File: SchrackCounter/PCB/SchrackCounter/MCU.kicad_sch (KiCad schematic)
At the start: 0 parts

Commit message: update
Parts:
- added C?: 100nF.mcu, Capacitor_SMD:C_0805_2012Metric_Pad1.18x1.45mm_HandSolder, symbol Device:C
- added C?: 10uF.mcu, Capacitor_Tantalum_SMD:CP_EIA-3216-18_Kemet-A_Pad1.58x1.35mm_HandSolder, symbol Device:C_Polarized
- added U?: ESP32-S3-WROOM-1, PCM_Espressif:ESP32-S3-WROOM-1, symbol sumec_sch_lib:ESP32-S3-WROOM-1_CUSTOM_made_by_bismarx
- added U?: ESP32-S3-WROOM-2, PCM_Espressif:ESP32-S3-WROOM-2, symbol PCM_Espressif:ESP32-S3-WROOM-2
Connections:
- new net: U?.1 (GND), U?.40 (GND), U?.41 (GND)
- new net +3V3: C?.1, C?.1, U?.2 (3V3)
- new net BOOT: U?.27 (IO0)
- new net D+: U?.14 (IO20)
- new net D-: U?.13 (IO19)
- new net EN: U?.3 (EN)
- new net GND: C?.2, C?.2, U?.1 (GND), U?.40 (GND), U?.41 (GND)
- new net IN1: U?.33 (IO40)
- new net IN2: U?.34 (IO41)
- new net IPROPI_ADC: U?.29 (IO36)
- new net IR MODULE: U?.28 (IO35)
- new net LED1: U?.23 (IO21)
- new net LED2: U?.22 (IO14)
- new net LED3: U?.21 (IO13)
- new net OUT 1A: U?.18 (IO10)
- new net OUT 1B: U?.17 (IO9)
- new net OUT 2A: U?.19 (IO11)
- new net OUT 2B: U?.20 (IO12)
- new net POL 1: U?.5 (IO5)
- new net POL 2: U?.8 (IO15)
- new net POL 3: U?.9 (IO16)
- new net PWM1: U?.35 (IO42)
- new net PWM2: U?.32 (IO39)
- new net QRE1113 A: U?.6 (IO6)
- new net QRE1113 B: U?.7 (IO7)
- new net QRE1113 C: U?.38 (IO2)
- new net RX: U?.36 (RXD0)
- new net SCL: U?.11 (IO18)
- new net SDA: U?.10 (IO17)
- new net SHARP 1: U?.12 (IO8)
- new net SHARP 2: U?.4 (IO4)
- new net TEST PROGRAM 1: U?.25 (IO48)
- new net TEST PROGRAM 2: U?.24 (IO47)
- new net TX: U?.37 (TXD0)
- new net nFAULT: U?.30 (IO37)
- new net nSLEEP: U?.31 (IO38)
- no-connect marks 0 -> 3
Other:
- note added: "Default Configuration of Strapping Pins Strapping Pin Default Configuration Bit Value GPIO0 Pull-up 1 GPIO3 Floating - GPIO45 Pull-down 0 GPIO46 Pull-down 0"
- note added: "ESP32-S3 Datasheet"
- note added: "ESP32-S3-WROOM1-N4"
- note added: "GPIO0 has an internal pullup resistor, so if it is left unconnected then it will pull high."
- note added: "GPIO0, GPIO45, and GPIO46 are connected to the chip's internal weak pull-up/pull-down resistors at chip reset. These resistors determine the default bit values of the strapping pins. Also, these resistors determine the bit values if the strapping pins are connected to an external high-impedance circuit."
- note added: "TEST!!!"
- note added: "Typically these can be used, but you need to make sure they are not in the wrong state during boot. gpio.0 Boot Mode. Weak pullup during reset. (Boot Mode 0=Boot from Flash, 1=Download) gpio.3 JTAG Mode. Weak pull down during reset. (JTAG Config) gpio.45 SPI voltage. Weak pull down during reset. (SPI Voltage 0=3.3v 1=1.8v) gpio.46 Boot mode. Weak pull down during reset. (Enabling/Disabling ROM Me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"
- note added: "working voltage for pins 47 and 48 is 1.8 (test it) Check pins with datasheet, ADC, SP, USB etc Check encoder connection UART connection?"

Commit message: Schematic update
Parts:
- removed U?: ESP32-S3-WROOM-1, PCM_Espressif:ESP32-S3-WROOM-1, symbol sumec_sch_lib:ESP32-S3-WROOM-1_CUSTOM_made_by_bismarx
- removed U?: ESP32-S3-WROOM-2, PCM_Espressif:ESP32-S3-WROOM-2, symbol PCM_Espressif:ESP32-S3-WROOM-2
- added U7: ESP32-S3-WROOM-2, PCM_Espressif:ESP32-S3-WROOM-2, symbol sumec_sch_lib:ESP32-S3-WROOM-2_CUSTOM_made_by_bismarx
- gave numbers to parts that had none: 2
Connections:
- net +3V3: now also U7.2 (3V3)
- net BOOT: now also U7.27 (IO0)
- net EN: now also U7.3 (EN)
- net GND: now also U7.1 (GND), U7.40 (GND), U7.41 (GND)
- no-connect marks 3 -> 2
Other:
- note removed: "TEST!!!"
- moved on the sheet: C11, C12

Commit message: Schematic update
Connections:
- net D-: now reaches U7.13 (IO19)
- net D+: now reaches U7.14 (IO20)
- net ~{CS}: now reaches U7.18 (IO10)
- net MOSI: now reaches U7.19 (IO11)
- net CLK: now reaches U7.20 (IO12)
- net RX: now reaches U7.36 (RXD0)
- net TX: now reaches U7.37 (TXD0)
- no-connect marks 2 -> 3
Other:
- note added: "ESP32-S3-WROOM2"
- note removed: "ESP32-S3-WROOM1-N4"
- note removed: "working voltage for pins 47 and 48 is 1.8 (test it) Check pins with datasheet, ADC, SP, USB etc Check encoder connection UART connection?"
- moved on the sheet: C11, C12, U7

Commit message: sleep, overated imo
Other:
- note added: "GPIO0 has an internal pullup resistor, so if it is left unconnected then it will pull high. GPIO0, GPIO45, and GPIO46 are connected to the chip's internal weak pull-up/pull-down resistors at chip reset. These resistors determine the default bit values of the strapping pins. Also, these resistors determine the bit values if the strapping pins are connected to an external high-impedance circuit."
- note removed: "GPIO0 has an internal pullup resistor, so if it is left unconnected then it will pull high."
- note removed: "GPIO0, GPIO45, and GPIO46 are connected to the chip's internal weak pull-up/pull-down resistors at chip reset. These resistors determine the default bit values of the strapping pins. Also, these resistors determine the bit values if the strapping pins are connected to an external high-impedance circuit."
- moved on the sheet: C11, C12, U7

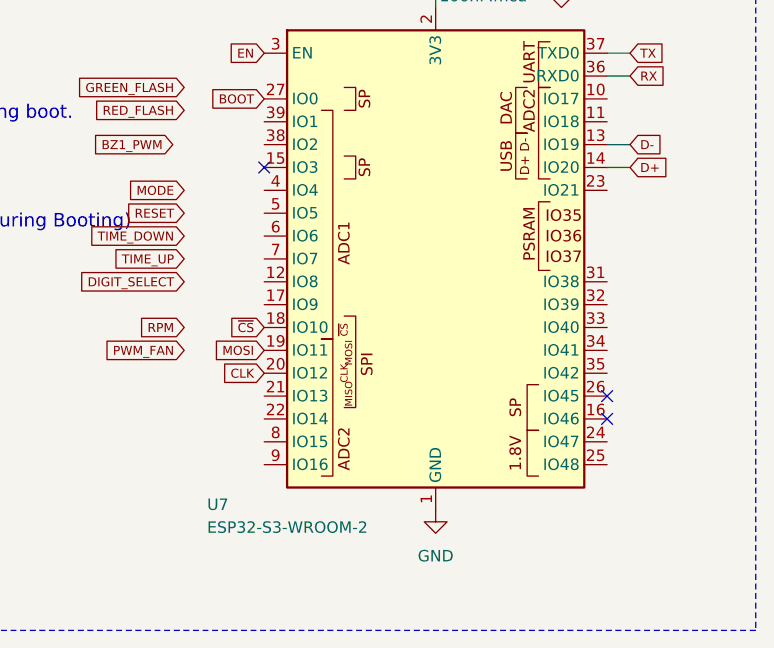
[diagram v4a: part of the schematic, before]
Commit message: SD card addition
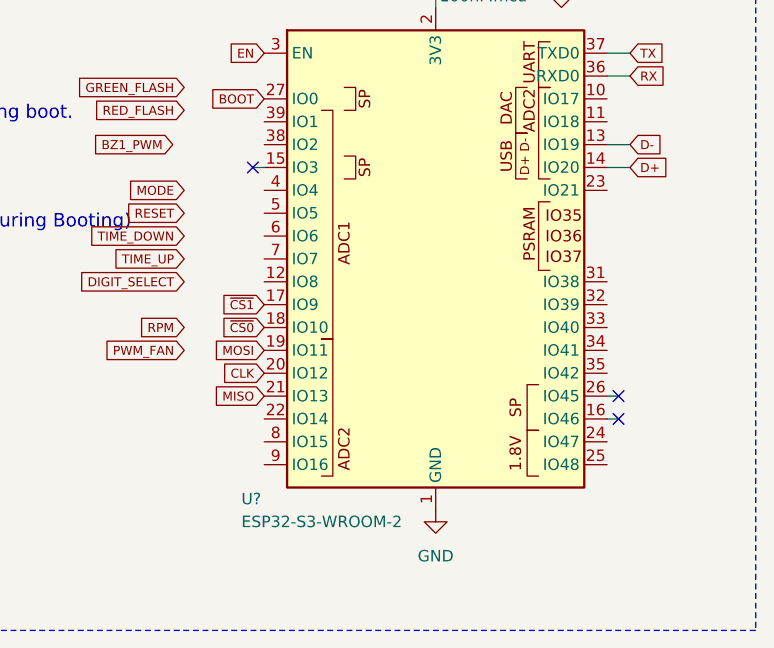
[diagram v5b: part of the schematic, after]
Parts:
- removed U7: ESP32-S3-WROOM-2, PCM_Espressif:ESP32-S3-WROOM-2, symbol sumec_sch_lib:ESP32-S3-WROOM-2_CUSTOM_made_by_bismarx
- added U?: ESP32-S3-WROOM-2, PCM_Espressif:ESP32-S3-WROOM-2, symbol sumec_sch_lib:ESP32-S3-WROOM-2_CUSTOM_made_by_bismarx
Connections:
- net +3V3: now also U?.2 (3V3)
- net BOOT: now also U?.27 (IO0)
- net CLK: now also U?.20 (IO12)
- net D+: now also U?.14 (IO20)
- net D-: now also U?.13 (IO19)
- net EN: now also U?.3 (EN)
- net GND: now also U?.1 (GND), U?.40 (GND), U?.41 (GND)
- net MOSI: now also U?.19 (IO11)
- net RX: now also U?.36 (RXD0)
- net TX: now also U?.37 (TXD0)
- new net MISO: U?.21 (IO13)
- new net ~{CS0}: U?.18 (IO10)
- new net ~{CS1}: U?.17 (IO9)
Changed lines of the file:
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@@
 	)
 	(no_connect
-		(at 217.17 114.3)
+		(at 218.44 114.3)
 	)
 	(no_connect
-		(at 179.07 86.36)
+		(at 177.8 86.36)
 	)
 	(no_connect
-		(at 217.17 111.76)
+		(at 218.44 111.76)
 	)
 	(wire
@@
 	(wire
 		(pts
+			(xy 218.44 111.76) (xy 217.17 111.76)
+		)
+		(stroke
+			(width 0)
+			(type default)
+		)
+	)
+	(wire
+		(pts
 			(xy 198.12 55.88) (xy 198.12 63.5)
 		)
@@
 		(pts
 			(xy 198.12 53.34) (xy 198.12 55.88)
+		)
+		(stroke
+			(width 0)
+			(type default)
+		)
+	)
+	(wire
+		(pts
+			(xy 177.8 86.36) (xy 179.07 86.36)
+		)
+		(stroke
+			(width 0)
+			(type default)
+		)
+	)
+	(wire
+		(pts
+			(xy 218.44 114.3) (xy 217.17 114.3)
 		)
 		(stroke
@@
 		)
 	)
-	(global_label "~{CS}"
+	(global_label "~{CS0}"
 		(shape input)
 		(at 179.07 104.14 180)
@@
 		)
 		(property "Intersheetrefs" "${INTERSHEET_REFS}"
-			(at 175.1948 104.14 0)
+			(at 174.4504 104.14 0)
 			(effects
 				(font
@@
 		)
 	)
+	(global_label "~{CS1}"
+		(shape input)
+		(at 179.07 101.6 180)
+		(fields_autoplaced yes)
+		(effects
+			(font
+				(face "Bahnschrift")
+				(size 1 1)
+				(color 0 0 0 1)
+			)
+			(justify right)
+		)
+		(property "Intersheetrefs" "${INTERSHEET_REFS}"
+			(at 174.7298 101.6 0)
+			(effects
+				(font
+					(size 1.27 1.27)
+				)
+				(justify right)
+				(hide yes)
+			)
+		)
+	)
 	(global_label "DIGIT_SELECT"
 		(shape input)
@@
 		)
 	)
+	(global_label "MISO"
+		(shape input)
+		(at 179.07 111.76 180)
+		(fields_autoplaced yes)
+		(effects
+			(font
+				(face "Bahnschrift")
+				(size 1 1)
+				(color 0 0 0 1)
+			)
+			(justify right)
+		)
+		(property "Intersheetrefs" "${INTERSHEET_REFS}"
+			(at 173.6815 111.76 0)
+			(effects
+				(font
+					(size 1.27 1.27)
+				)
+				(justify right)
+				(hide yes)
+			)
+		)
+	)
 	(global_label "TIME_UP"
 		(shape input)
@@
 				(justify right)
 				(hide yes)
+			)
+		)
+	)
+	(symbol
+		(lib_id "sumec_sch_lib:ESP32-S3-WROOM-2_CUSTOM_made_by_bismarx")
+		(at 201.93 96.52 0)
+		(unit 1)
+		(exclude_from_sim no)
+		(in_bom yes)
+		(on_board yes)
+		(dnp no)
+		(property "Reference" "U?"
+			(at 176.53 123.19 0)
+			(effects
+				(font
+					(size 1.27 1.27)
+				)
+				(justify left)
+			)
+		)
+		(property "Value" "ESP32-S3-WROOM-2"
+			(at 176.53 125.73 0)
+			(effects
+				(font
+					(size 1.27 1.27)
+				)
+				(justify left)
+			)
+		)
+		(property "Footprint" "PCM_Espressif:ESP32-S3-WROOM-2"
+			(at 199.136 53.086 0)
+			(effects
+				(font
+					(size 1.27 1.27)
+				)
+				(hide yes)
+			)
+		)
+		(property "Datasheet" "https://www.espressif.com/sites/default/files/documentation/esp32-s3-wroom-1_wroom-1u_datasheet_en.pdf"
+			(at 198.374 59.182 0)
+			(effects
+				(font
+					(size 1.27 1.27)
+				)
+				(hide yes)
+			)
+		)
+		(property "Description" "RF Module, ESP32-S3 SoC, Wi-Fi 802.11b/g/n, Bluetooth, BLE, 32-bit, 3.3V, onboard antenna, SMD"
+			(at 199.39 56.134 0)
+			(effects
+				(font
+					(size 1.27 1.27)
+				)
+				(hide yes)
+			)
+		)
+		(pin "40"
+		)
+		(pin "20"
+		)
+		(pin "27"
+		)
+		(pin "16"
+		)
+		(pin "23"
+		)
+		(pin "26"
+		)
+		(pin "12"
+		)
+		(pin "10"
+		)
+		(pin "4"
+		)
+		(pin "25"
+		)
+		(pin "41"
+		)
+		(pin "24"
+		)
+		(pin "19"
+		)
+		(pin "34"
+		)
+		(pin "33"
+		)
+		(pin "37"
+		)
+		(pin "38"
+		)
+		(pin "13"
+		)
+		(pin "14"
+		)
+		(pin "21"
+		)
+		(pin "32"
+		)
+		(pin "11"
+		)
+		(pin "22"
+		)
+		(pin "39"
+		)
+		(pin "7"
+		)
+		(pin "2"
+		)
+		(pin "6"
+		)
+		(pin "15"
+		)
+		(pin "31"
+		)
+		(pin "35"
+		)
+		(pin "36"
+		)
+		(pin "18"
+		)
+		(pin "1"
+		)
+		(pin "8"
+		)
+		(pin "9"
+		)
+		(pin "5"
+		)
+		(pin "3"
+		)
+		(pin "17"
+		)
+		(instances
+			(project ""
+				(path "/d96f2ffc-3f4c-4f71-b693-29f6b8c3245d/39e148ed-9462-493d-862b-d9debebaa239"
+					(reference "U?")
+					(unit 1)
+				)
 			)
 		)
@@
 					(unit 1)
 				)
-			)
-		)
-	)
-	(symbol
-		(lib_id "sumec_sch_lib:ESP32-S3-WROOM-2_CUSTOM_made_by_bismarx")
-		(at 201.93 96.52 0)
-		(unit 1)
-		(exclude_from_sim no)
-		(in_bom yes)
-		(on_board yes)
-		(dnp no)
-		(property "Reference" "U7"
-			(at 172.72 123.825 0)
-			(effects
-				(font
-					(size 1.27 1.27)
-				)
-				(justify left)
-			)
-		)
-		(property "Value" "ESP32-S3-WROOM-2"
-			(at 172.72 126.365 0)
-			(effects
-				(font
-					(size 1.27 1.27)
-				)
-				(justify left)
-			)
-		)
-		(property "Footprint" "PCM_Espressif:ESP32-S3-WROOM-2"
-			(at 199.136 53.086 0)
-			(effects
-				(font
-					(size 1.27 1.27)
-				)
-				(hide yes)
-			)
-		)
-		(property "Datasheet" "https://www.espressif.com/sites/default/files/documentation/esp32-s3-wroom-1_wroom-1u_datasheet_en.pdf"
-			(at 198.374 59.182 0)
-			(effects
-				(font
-					(size 1.27 1.27)
-				)
-				(hide yes)
-			)
-		)
-		(property "Description" "RF Module, ESP32-S3 SoC, Wi-Fi 802.11b/g/n, Bluetooth, BLE, 32-bit, 3.3V, onboard antenna, SMD"
-			(at 199.39 56.134 0)
-			(effects
-				(font
-					(size 1.27 1.27)
-				)
-				(hide yes)
-			)
-		)
-		(pin "22"
-		)
-		(pin "1"
-		)
-		(pin "6"
-		)
-		(pin "25"
-		)
-		(pin "8"
-		)
-		(pin "18"
-		)
-		(pin "27"
-		)
-		(pin "2"
-		)
-		(pin "19"
-		)
-		(pin "33"
-		)
-		(pin "20"
-		)
-		(pin "17"
-		)
-		(pin "32"
-		)
-		(pin "24"
-		)
-		(pin "13"
-		)
-		(pin "36"
-		)
-		(pin "16"
-		)
-		(pin "23"
-		)
-		(pin "15"
-		)
-		(pin "3"
-		)
-		(pin "38"
-		)
-		(pin "26"
-		)
-		(pin "11"
-		)
-		(pin "21"
-		)
-		(pin "35"
-		)
-		(pin "5"
-		)
-		(pin "4"
-		)
-		(pin "14"
-		)
-		(pin "31"
-		)
-		(pin "39"
-		)
-		(pin "41"
-		)
-		(pin "40"
-		)
-		(pin "7"
-		)
-		(pin "12"
-		)
-		(pin "9"
-		)
-		(pin "10"
-		)
-		(pin "34"
-		)
-		(pin "37"
-		)
-		(instances
-			(project ""
-				(path "/d96f2ffc-3f4c-4f71-b693-29f6b8c3245d/39e148ed-9462-493d-862b-d9debebaa239"
-					(reference "U7")
-					(unit 1)
-				)

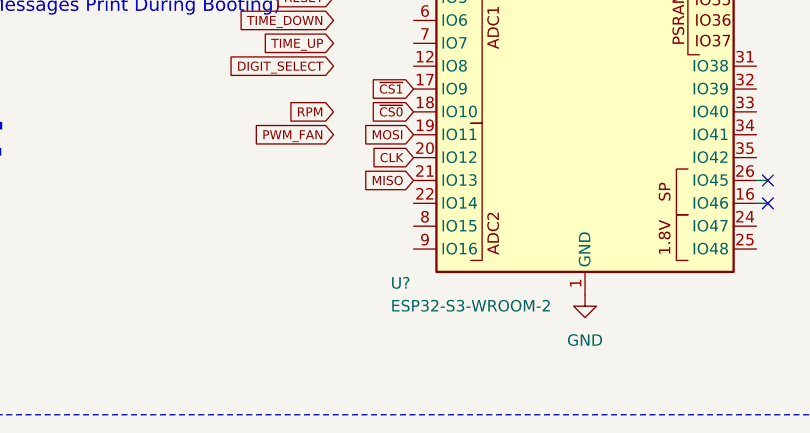
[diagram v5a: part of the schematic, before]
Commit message: Footprint reorder, schematic and pcb update
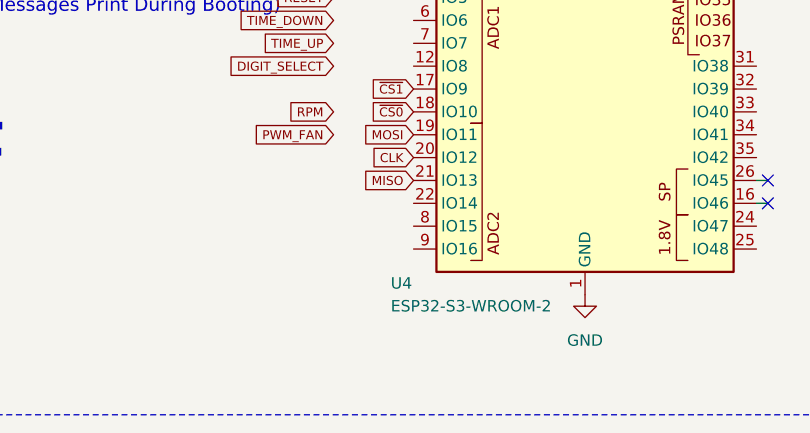
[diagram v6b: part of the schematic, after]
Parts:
- gave numbers to parts that had none: 1
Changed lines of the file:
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@@
 		(on_board yes)
 		(dnp no)
-		(property "Reference" "U?"
+		(property "Reference" "U4"
 			(at 176.53 123.19 0)
 			(effects
@@
 			(project ""
 				(path "/d96f2ffc-3f4c-4f71-b693-29f6b8c3245d/39e148ed-9462-493d-862b-d9debebaa239"
-					(reference "U?")
+					(reference "U4")
 					(unit 1)
 				)

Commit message: PCB update
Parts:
- renumbered U4 to U5

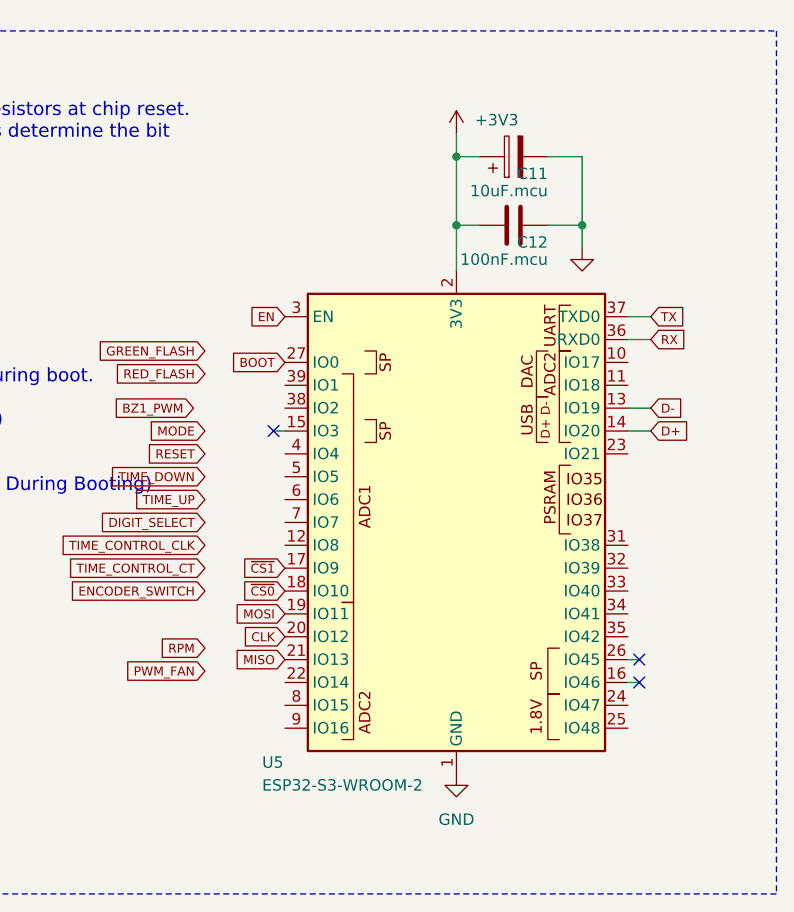
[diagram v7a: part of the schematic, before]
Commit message: Schematic and PCB update
LDO Regulator, and some layout update
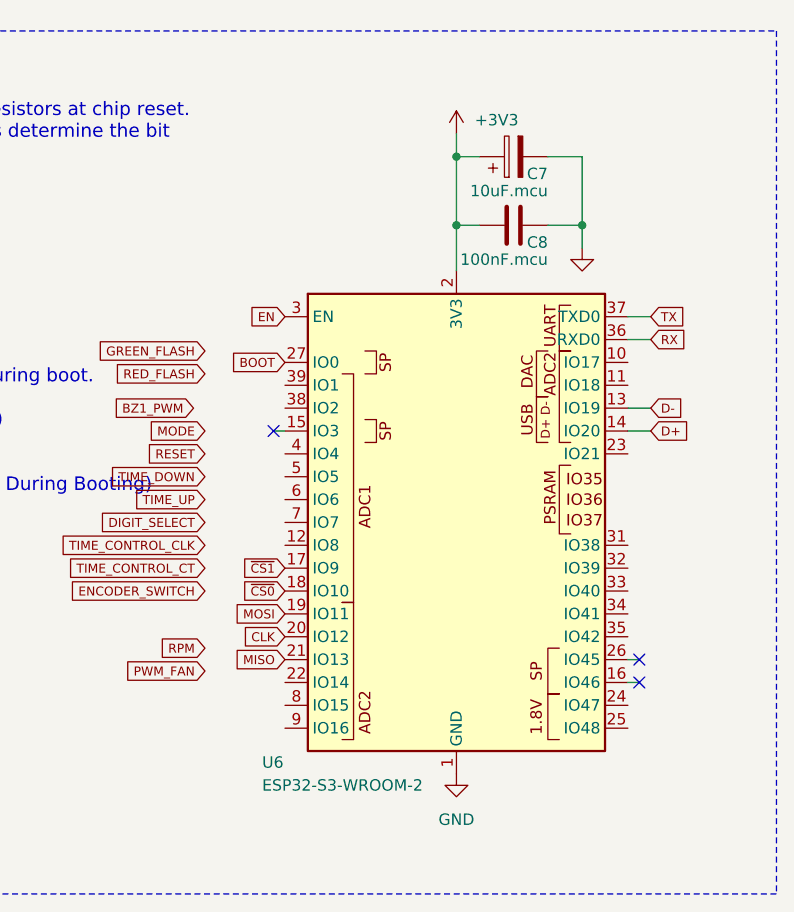
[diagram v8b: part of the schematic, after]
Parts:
- renumbered C11 to C7, C12 to C8, U5 to U6
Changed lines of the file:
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@@
 		(on_board yes)
 		(dnp no)
-		(property "Reference" "U5"
+		(property "Reference" "U6"
 			(at 176.53 123.19 0)
 			(effects
@@
 			(project ""
 				(path "/d96f2ffc-3f4c-4f71-b693-29f6b8c3245d/39e148ed-9462-493d-862b-d9debebaa239"
-					(reference "U5")
+					(reference "U6")
 					(unit 1)
 				)
@@
 		(on_board yes)
 		(dnp no)
-		(property "Reference" "C12"
+		(property "Reference" "C8"
 			(at 208.28 65.405 90)
 			(effects
@@
 			(project "SchrackCounter"
 				(path "/d96f2ffc-3f4c-4f71-b693-29f6b8c3245d/39e148ed-9462-493d-862b-d9debebaa239"
-					(reference "C12")
+					(reference "C8")
 					(unit 1)
 				)
@@
 		(on_board yes)
 		(dnp no)
-		(property "Reference" "C11"
+		(property "Reference" "C7"
 			(at 208.28 57.785 90)
 			(effects
@@
 			(project "SchrackCounter"
 				(path "/d96f2ffc-3f4c-4f71-b693-29f6b8c3245d/39e148ed-9462-493d-862b-d9debebaa239"
-					(reference "C11")
+					(reference "C7")
 					(unit 1)
 				)
@@
 		(on_board yes)
 		(dnp no)
-		(property "Reference" "#PWR021"
+		(property "Reference" "#PWR015"
 			(at 198.12 57.15 0)
 			(effects
@@
 			(project "SchrackCounter"
 				(path "/d96f2ffc-3f4c-4f71-b693-29f6b8c3245d/39e148ed-9462-493d-862b-d9debebaa239"
-					(reference "#PWR021")
+					(reference "#PWR015")
 					(unit 1)
 				)
@@
 		(dnp no)
 		(fields_autoplaced yes)
-		(property "Reference" "#PWR022"
+		(property "Reference" "#PWR016"
 			(at 198.12 130.81 0)
 			(effects
@@
 			(project ""
 				(path "/d96f2ffc-3f4c-4f71-b693-29f6b8c3245d/39e148ed-9462-493d-862b-d9debebaa239"
-					(reference "#PWR022")
+					(reference "#PWR016")
 					(unit 1)
 				)
@@
 		(dnp no)
 		(fields_autoplaced yes)
-		(property "Reference" "#PWR023"
+		(property "Reference" "#PWR017"
 			(at 212.09 72.39 0)
 			(effects
@@
 			(project "SchrackCounter"
 				(path "/d96f2ffc-3f4c-4f71-b693-29f6b8c3245d/39e148ed-9462-493d-862b-d9debebaa239"
-					(reference "#PWR023")
-					(unit 1)
-				)
+					(reference "#PWR017")
+					(unit 1)
+				)
